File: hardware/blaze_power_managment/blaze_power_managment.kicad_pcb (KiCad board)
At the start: 4 copper layers, 70 x 70 mm, 62 parts, among them J1 Conn_01x30_Pin, J2 Conn_01x30_Socket, J3 XT30, J4 XT30, J5 JTAG, Q1 DMG2305, SW1 SW_SPST, SW2 SW_SPDT, U1 TCAN1044VDDFR, U2 TPS62913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

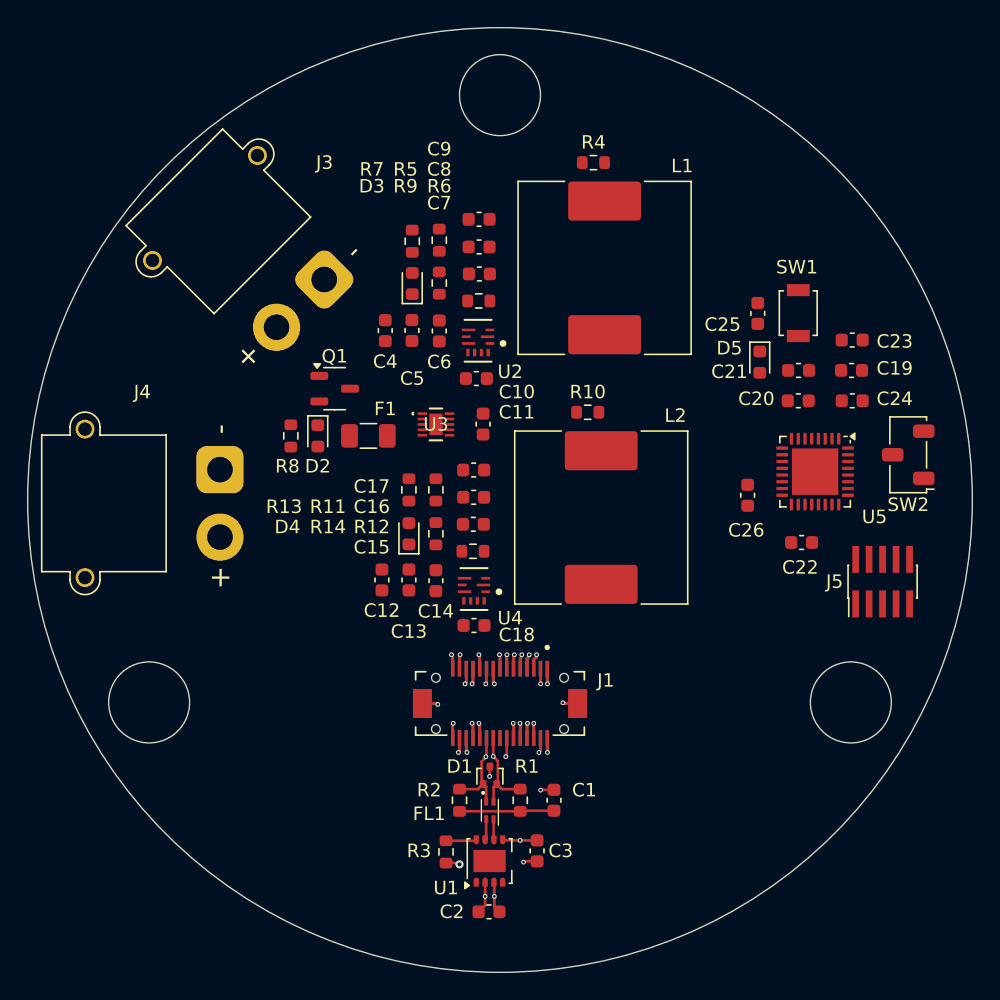
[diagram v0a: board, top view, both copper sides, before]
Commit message: Completed initial routing
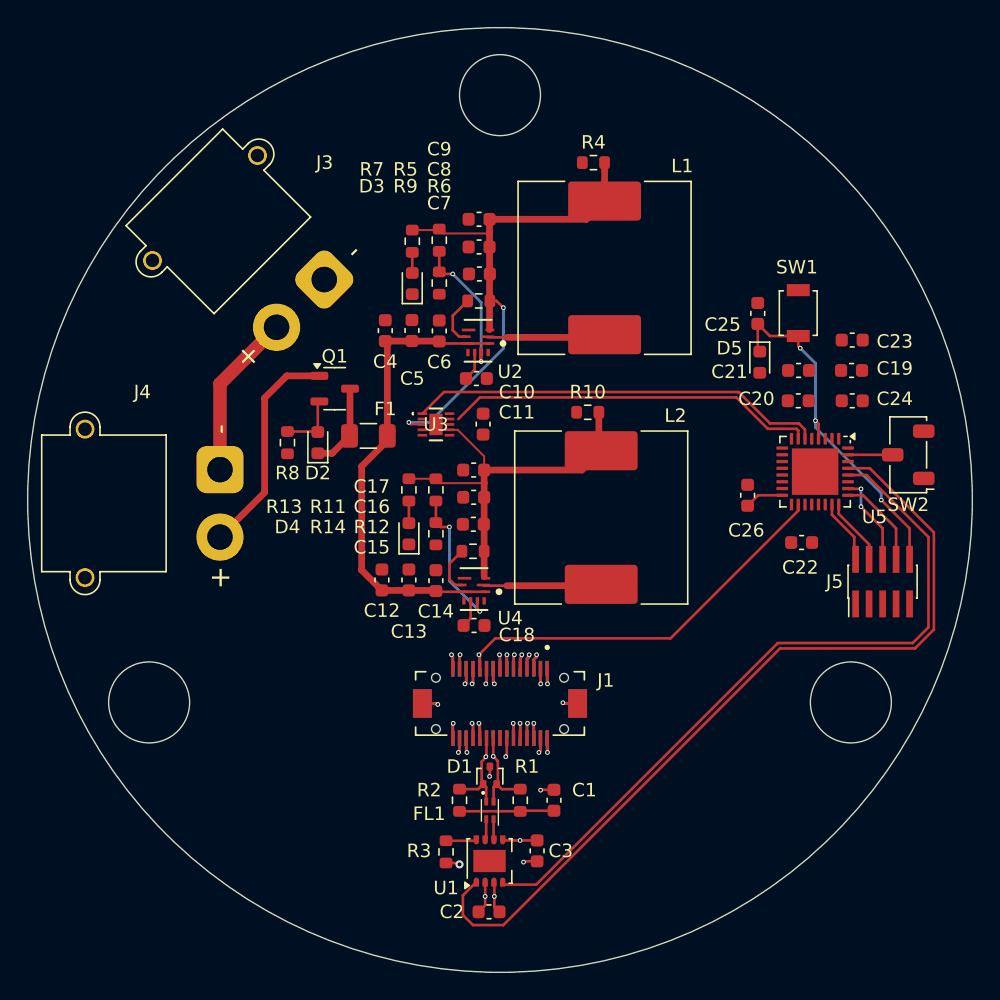
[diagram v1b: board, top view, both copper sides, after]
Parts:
- J1: value Conn_01x30_Pin -> FrontInterconnect
- J2: value Conn_01x30_Socket -> RearInterconnect
- moved R8 0.56 mm to (132.8, 101.2), turned to -90 degrees
- moved D2 0.50 mm to (135.0, 101.2), turned to 90 degrees
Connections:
- C15 pad 1: /3V3_SENSE -> /3V3_SENSE_IN
- C16 pad 1: /3V3_SENSE -> /3V3_SENSE_IN
- C17 pad 1: /3V3_SENSE -> /3V3_SENSE_IN
- C7 pad 1: /5V_SENSE -> /5V_SENSE_IN
- C8 pad 1: /5V_SENSE -> /5V_SENSE_IN
- C9 pad 1: /5V_SENSE -> /5V_SENSE_IN
- J1 pad 1: VBATT -> GND
- J1 pad 10: Net-(J1-Pin_10) -> +3V3
- J1 pad 11: +5V -> /PPS
- J1 pad 12: +3V3 -> GND
- J1 pad 13: /PPS -> GND
- J1 pad 14: GND -> Net-(J1-Pin_14)
- J1 pad 15: GND -> Net-(J1-Pin_15)
- J1 pad 16: Net-(J1-Pin_16) -> +3V3
- J1 pad 18: +3V3 -> Net-(J1-Pin_18)
- J1 pad 19: Net-(J1-Pin_19) -> GND
- J1 pad 2: VBATT -> GND
- J1 pad 20: Net-(J1-Pin_20) -> GND
- J1 pad 21: GND -> /CANH
- J1 pad 22: GND -> /CANL
- J1 pad 23: /CANL -> Net-(J1-Pin_23)
- J1 pad 24: /CANH -> Net-(J1-Pin_24)
- J1 pad 25: Net-(J1-Pin_25) -> +5V
- J1 pad 26: Net-(J1-Pin_26) -> +5V
- J1 pad 27: +5V -> +3V3
- J1 pad 28: +5V -> +3V3
- J1 pad 29: +3V3 -> Net-(J1-Pin_29)
- J1 pad 3: GND -> /TX_RADIO
- J1 pad 30: +3V3 -> Net-(J1-Pin_30)
- J1 pad 4: GND -> /RX_RADIO
- J1 pad 6: Net-(J1-Pin_6) -> /ARM
- J1 pad 8: /ARM -> Net-(J1-Pin_8)
- J1 pad 9: Net-(J1-Pin_9) -> +5V
- J1 pad S1: (no net) -> GND
- J1 pad S2: (no net) -> GND
- J2 pad 1: +3V3 -> Net-(J1-Pin_30)
- J2 pad 10: GND -> /CANH
- J2 pad 11: Net-(J1-Pin_20) -> GND
- J2 pad 12: Net-(J1-Pin_19) -> GND
- J2 pad 13: +3V3 -> Net-(J1-Pin_18)
- J2 pad 15: Net-(J1-Pin_16) -> +3V3
- J2 pad 16: GND -> Net-(J1-Pin_15)
- J2 pad 17: GND -> Net-(J1-Pin_14)
- J2 pad 18: /PPS -> GND
- J2 pad 19: +3V3 -> GND
- J2 pad 2: +3V3 -> Net-(J1-Pin_29)
- J2 pad 20: +5V -> /PPS
- J2 pad 21: Net-(J1-Pin_10) -> +3V3
- J2 pad 22: Net-(J1-Pin_9) -> +5V
- J2 pad 23: /ARM -> Net-(J1-Pin_8)
- J2 pad 25: Net-(J1-Pin_6) -> /ARM
- J2 pad 27: GND -> /RX_RADIO
- J2 pad 28: GND -> /TX_RADIO
- J2 pad 29: VBATT -> GND
- J2 pad 3: +5V -> +3V3
- J2 pad 30: VBATT -> GND
- J2 pad 4: +5V -> +3V3
- J2 pad 5: Net-(J1-Pin_26) -> +5V
- J2 pad 6: Net-(J1-Pin_25) -> +5V
- J2 pad 7: /CANH -> Net-(J1-Pin_24)
- J2 pad 8: /CANL -> Net-(J1-Pin_23)
- J2 pad 9: GND -> /CANL
- J2 pad S1: (no net) -> GND
- J2 pad S2: (no net) -> GND
- J3 pad 1: Net-(J3-Pin_1) -> GND
- J4 pad 2: GND -> Net-(J4-Pin_2)
- L1 pad 2: /5V_SENSE -> /5V_SENSE_IN
- L2 pad 2: /3V3_SENSE -> /3V3_SENSE_IN
- Q1 pad 1: Net-(J3-Pin_1) -> Net-(J4-Pin_2)
- R10 pad 1: /3V3_SENSE -> /3V3_SENSE_IN
- R11 pad 1: /3V3_SENSE -> /3V3_SENSE_IN
- R12 pad 2: /3V3_SENSE -> /3V3_SENSE_IN
- R13 pad 1: /3V3_SENSE -> /3V3_SENSE_IN
- R4 pad 1: /5V_SENSE -> /5V_SENSE_IN
- R5 pad 1: /5V_SENSE -> /5V_SENSE_IN
- R6 pad 2: /5V_SENSE -> /5V_SENSE_IN
- R7 pad 1: /5V_SENSE -> /5V_SENSE_IN
- U2 pad 3: /5V_SENSE -> /5V_SENSE_IN
- U4 pad 3: /3V3_SENSE -> /3V3_SENSE_IN
- U5 pad 6: /5V_SENSE -> /3V3_SENSE
- U5 pad 7: /3V3_SENSE -> /5V_SENSE
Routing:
- net /CANTX: track 0.00 -> 62.7 mm
- net /CANRX: track 0.00 -> 54.0 mm
- net /5V_SENSE_IN: track 0.00 -> 40.8 mm, vias 0 -> 2
- net VIN: track 0.00 -> 35.5 mm
- net /3V3_SENSE: track 0.00 -> 30.8 mm
- net /3V3_SENSE_IN: track 0.00 -> 30.2 mm
- net /PPS: track 2.33 -> 30.7 mm
- net /5V_SENSE: track 0.00 -> 27.5 mm
- net /RESET: track 0.00 -> 26.9 mm, vias 0 -> 3
- net Net-(J4-Pin_2): track 0.00 -> 16.4 mm
- net Net-(J3-Pin_2): track 0.00 -> 12.3 mm
- net Net-(U2-FB): track 0.00 -> 11.3 mm, vias 0 -> 2
- net Net-(U4-FB): track 0.00 -> 10.8 mm, vias 0 -> 2
- net Net-(U4-SW): track 0.00 -> 8.77 mm
- net Net-(U2-SW): track 0.00 -> 8.76 mm
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
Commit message: power routing
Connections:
- D1 pad 1: /CANL -> /CANH
- D1 pad 2: /CANH -> /CANL
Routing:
- net GND: track 23.2 -> 94.6 mm, vias 12 -> 32
- net +5V: track 26.6 -> 83.6 mm, vias 4 -> 9
- net +3V3: track 12.6 -> 46.4 mm, vias 6 -> 12
- net Net-(J1-Pin_23): track 0.00 -> 2.28 mm, vias 0 -> 1
- net /PPS: track 30.7 -> 32.6 mm
- net /5V_SENSE_IN: track 40.8 -> 42.3 mm
- net /CANH: track 6.94 -> 8.34 mm
- net /CANL: track 6.90 -> 8.25 mm
- net Net-(J1-Pin_24): track 1.40 -> 2.74 mm
- net /3V3_SENSE_IN: track 30.2 -> 31.5 mm
- net /5V_SENSE: track 27.5 -> 28.1 mm

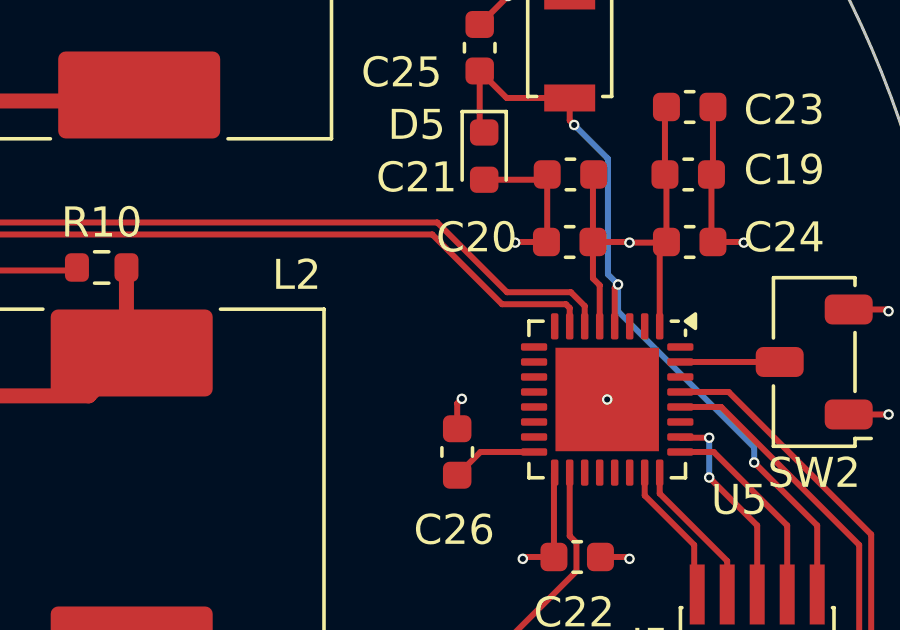
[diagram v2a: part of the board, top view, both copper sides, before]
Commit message: Added voltage sensing
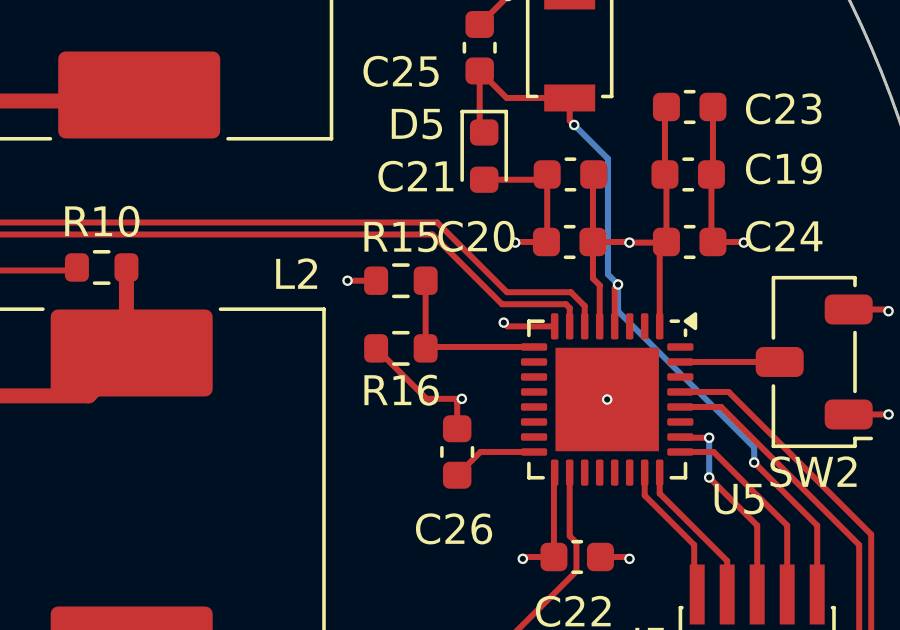
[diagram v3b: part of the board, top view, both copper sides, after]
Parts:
- added R15: 100k, Resistor_SMD:R_0603_1608Metric, F.Cu at (165.0, 99.4)
- added R16: 47k, Resistor_SMD:R_0603_1608Metric, F.Cu at (165.0, 101.7)
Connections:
- U5 pad 8: unconnected-(U5-PA2-Pad8) -> +3V3
- U5 pad 9: unconnected-(U5-PA3-Pad9) -> Net-(U5-PA3)
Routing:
- net +5V: track 83.6 -> 102.6 mm, vias 9 -> 10
- net Net-(U5-PA3): track 0.00 -> 5.89 mm
- net GND: track 94.6 -> 98.1 mm
- net +3V3: track 46.4 -> 48.1 mm, vias 12 -> 13
